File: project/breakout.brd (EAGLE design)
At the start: 20.3 x 30.5 mm, 2 parts

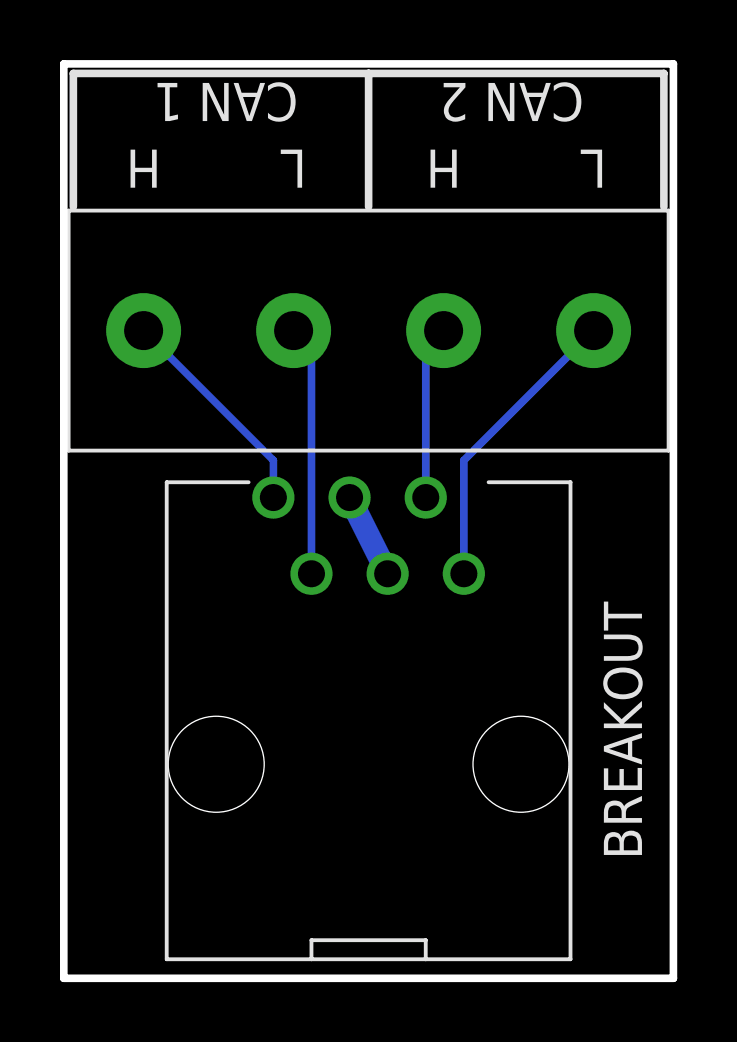
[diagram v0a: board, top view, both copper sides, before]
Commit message: Increase trace size
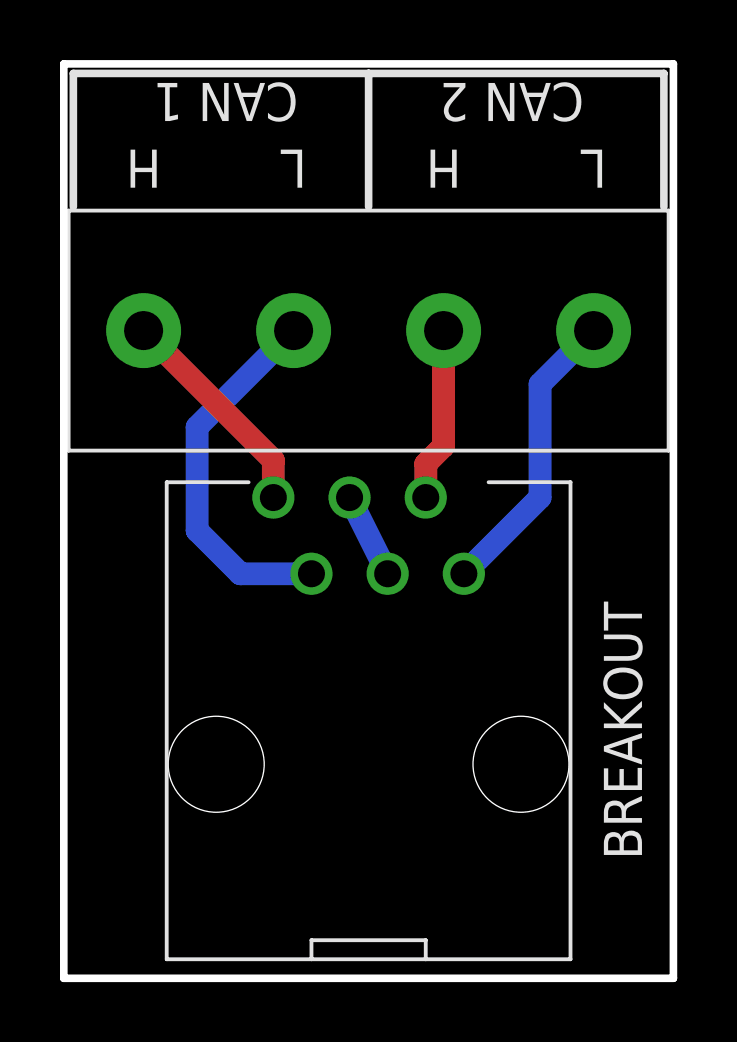
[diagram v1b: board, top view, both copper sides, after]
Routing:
- net N$3: track 8.35 -> 12.4 mm
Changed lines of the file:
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@@
 <contactref element="BREAKOUT" pad="1"/>
 <contactref element="U$1" pad="1"/>
-<wire x1="-3.175" y1="16.025" x2="-3.175" y2="17.265" width="0.254" layer="16"/>
-<wire x1="-3.175" y1="17.265" x2="-7.5" y2="21.59" width="0.254" layer="16"/>
+<wire x1="-7.5" y1="21.59" x2="-3.175" y2="17.265" width="0.762" layer="1"/>
+<wire x1="-3.175" y1="17.265" x2="-3.175" y2="16.025" width="0.762" layer="1"/>
 </signal>
 <signal name="N$3">
 <contactref element="BREAKOUT" pad="2"/>
 <contactref element="U$1" pad="2"/>
-<wire x1="-1.905" y1="13.485" x2="-1.905" y2="20.995" width="0.254" layer="16"/>
-<wire x1="-1.905" y1="20.995" x2="-2.5" y2="21.59" width="0.254" layer="16"/>
+<wire x1="-1.905" y1="13.485" x2="-4.2775" y2="13.485" width="0.762" layer="16"/>
+<wire x1="-4.2775" y1="13.485" x2="-5.715" y2="14.9225" width="0.762" layer="16"/>
+<wire x1="-5.715" y1="14.9225" x2="-5.715" y2="18.375" width="0.762" layer="16"/>
+<wire x1="-5.715" y1="18.375" x2="-2.5" y2="21.59" width="0.762" layer="16"/>
 </signal>
 <signal name="N$4">
 <contactref element="BREAKOUT" pad="5"/>
 <contactref element="U$1" pad="3"/>
-<wire x1="1.905" y1="16.025" x2="1.905" y2="20.995" width="0.254" layer="16"/>
-<wire x1="1.905" y1="20.995" x2="2.5" y2="21.59" width="0.254" layer="16"/>
+<wire x1="1.905" y1="16.025" x2="1.905" y2="17.145" width="0.762" layer="1"/>
+<wire x1="2.5" y1="21.59" x2="2.5" y2="17.74" width="0.762" layer="1"/>
+<wire x1="2.5" y1="17.74" x2="1.905" y2="17.145" width="0.762" layer="1"/>
 </signal>
 <signal name="N$5">
 <contactref element="BREAKOUT" pad="6"/>
 <contactref element="U$1" pad="4"/>
-<wire x1="3.175" y1="13.485" x2="3.175" y2="17.265" width="0.254" layer="16"/>
-<wire x1="3.175" y1="17.265" x2="7.5" y2="21.59" width="0.254" layer="16"/>
+<wire x1="3.175" y1="13.485" x2="5.715" y2="16.025" width="0.762" layer="16"/>
+<wire x1="5.715" y1="19.805" x2="7.5" y2="21.59" width="0.762" layer="16"/>
+<wire x1="5.715" y1="16.025" x2="5.715" y2="19.805" width="0.762" layer="16"/>
 </signal>
 </signals>
